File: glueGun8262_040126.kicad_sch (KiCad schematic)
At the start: 73 parts, among them CN1 KF243-5.0-2P, CN2 KF243-5.0-2P, CN3 KF243-5.0-2P, CN4 KF243-5.0-2P, CN5 KF243-5.0-2P, CN6 KF243-5.0-2P, CN7 KF243-5.0-2P, CN9 KF243-5.0-4P, Q1 SQM120P10-10m1L, U1 DRV8262DDWR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

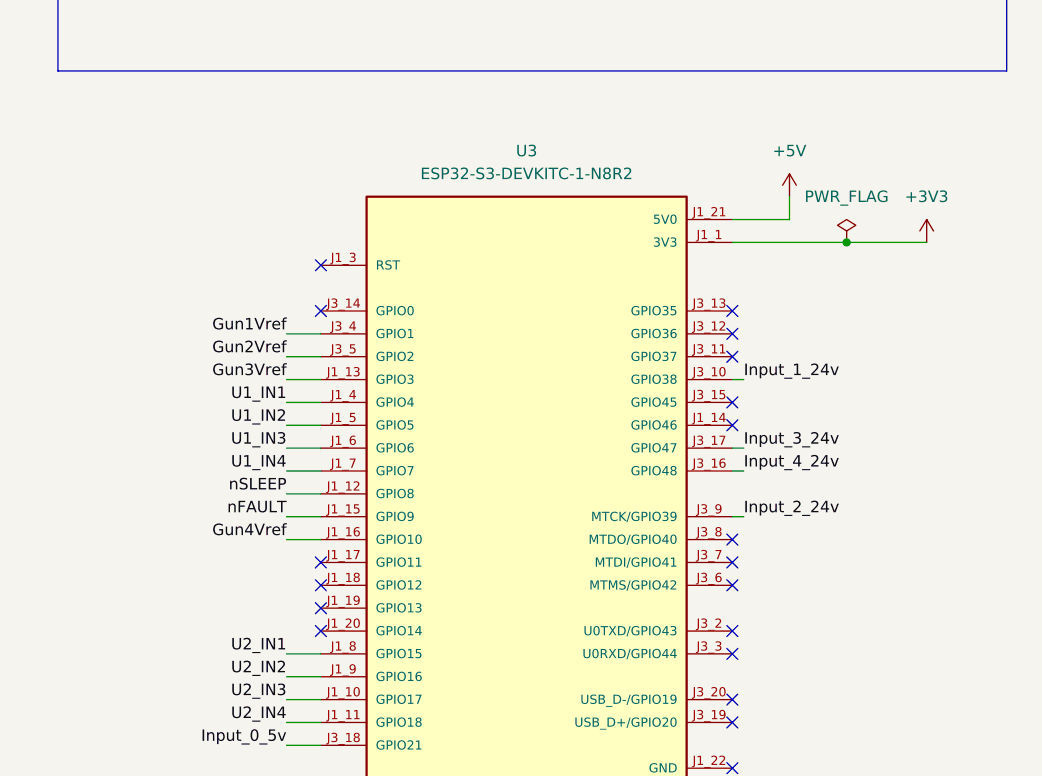
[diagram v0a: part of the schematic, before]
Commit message: schematics updated pinout
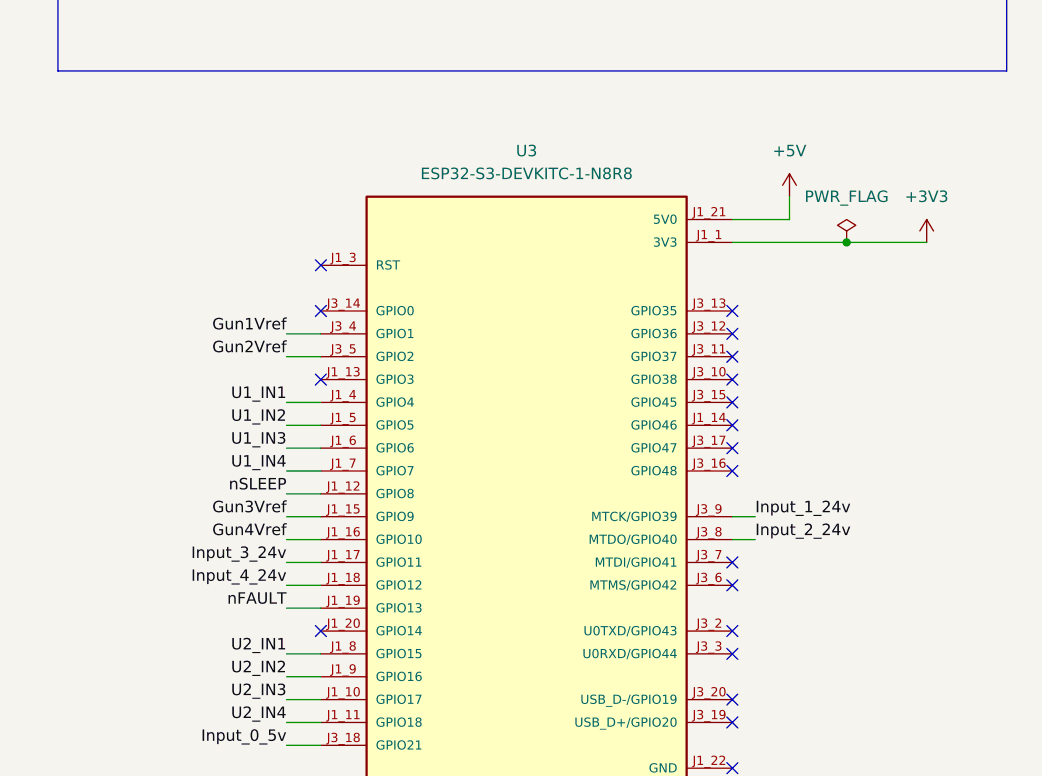
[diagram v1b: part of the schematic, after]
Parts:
- U3: value ESP32-S3-DEVKITC-1-N8R2 -> ESP32-S3-DEVKITC-1-N8R8
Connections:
- net Gun3Vref: now also U3.J1_15 (GPIO9); no longer U3.J1_13 (GPIO3)
- net Input_1_24v: now also U3.J3_9 (MTCK/GPIO39); no longer U3.J3_10 (GPIO38)
- net Input_2_24v: now also U3.J3_8 (MTDO/GPIO40); no longer U3.J3_9 (MTCK/GPIO39)
- net Input_3_24v: now also U3.J1_17 (GPIO11); no longer U3.J3_17 (GPIO47)
- net Input_4_24v: now also U3.J1_18 (GPIO12); no longer U3.J3_16 (GPIO48)
- net nFAULT: now also U3.J1_19 (GPIO13); no longer U3.J1_15 (GPIO9)

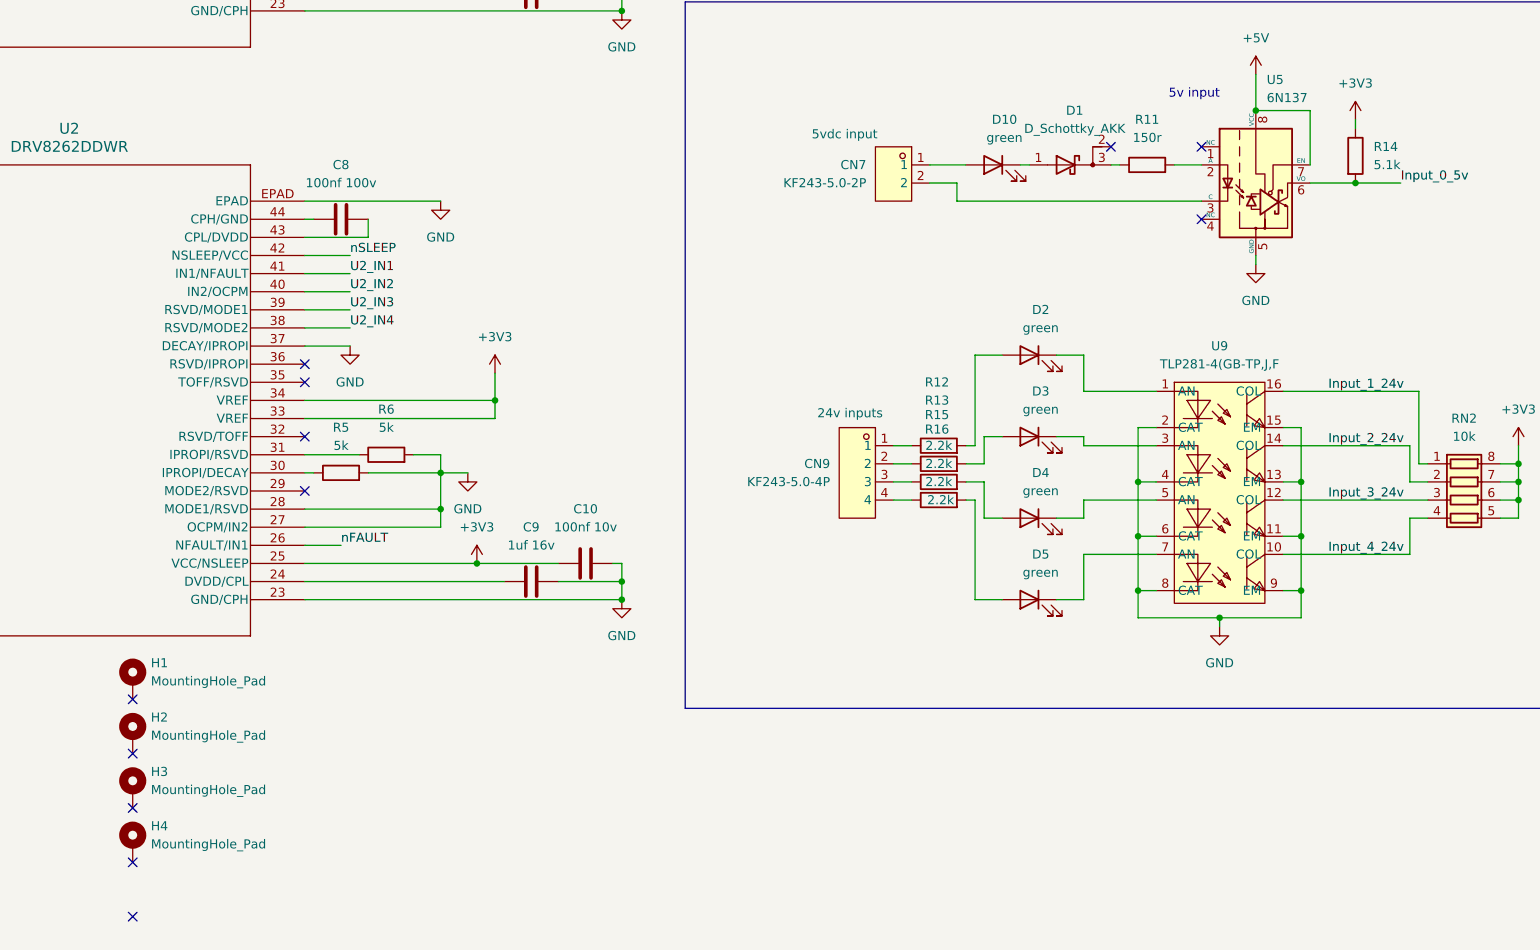
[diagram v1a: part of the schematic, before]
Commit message: pcb rewired new pinout
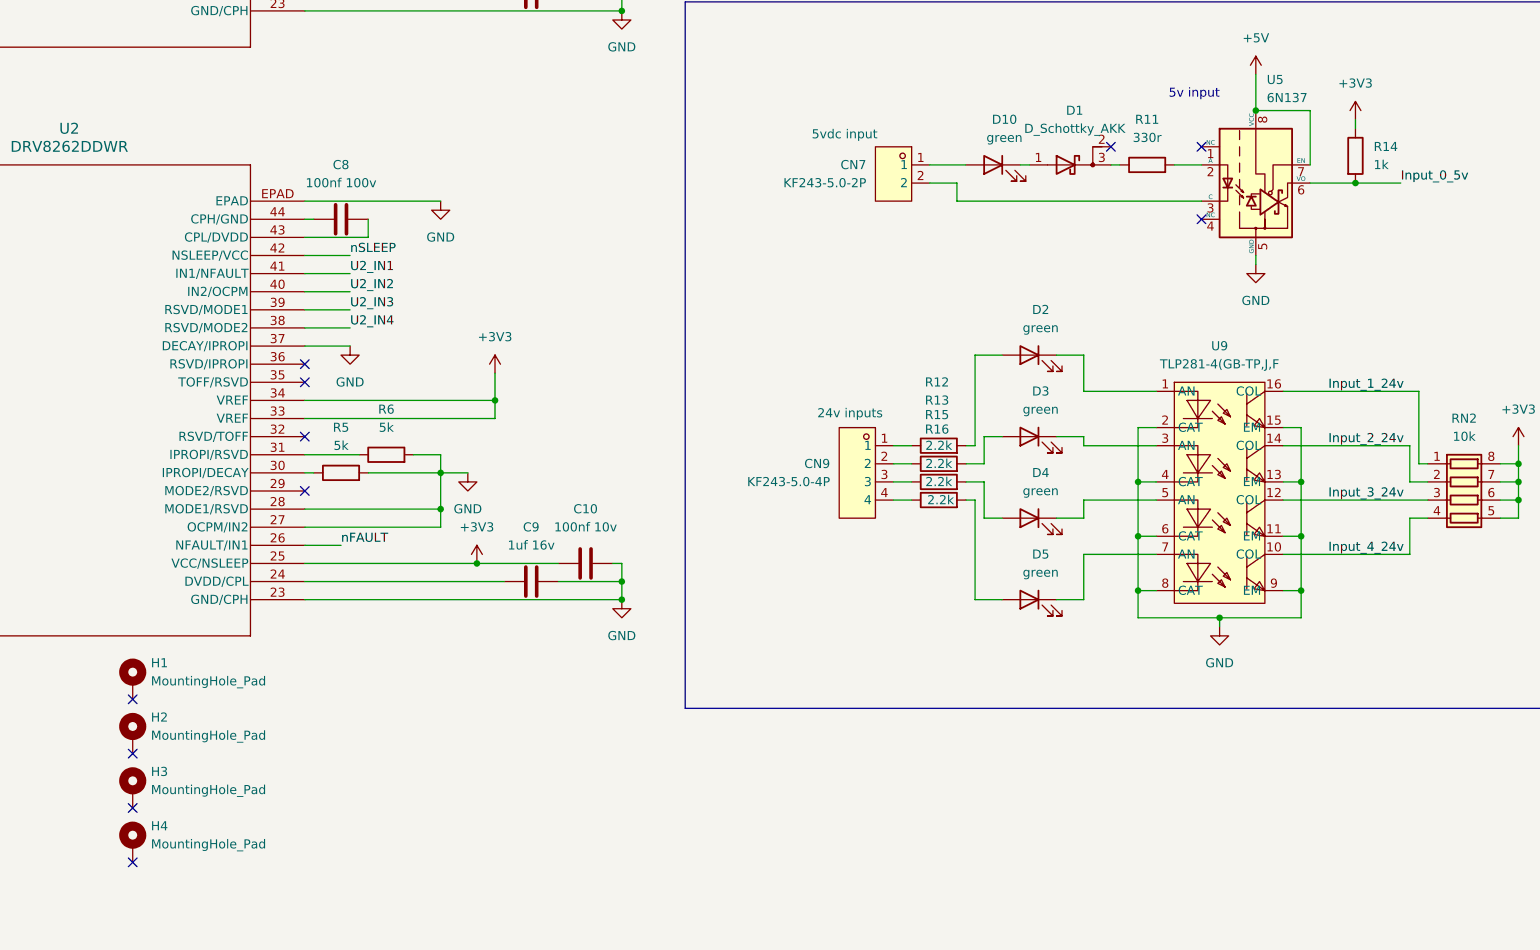
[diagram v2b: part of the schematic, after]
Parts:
- D1: footprint Package_TO_SOT_SMD:SOT-23 -> Diode_SMD:D_SOD-123; part (none) -> ss14
- D11: part (none) -> ss26
- D14: footprint (none) -> Diode_SMD:D_SMA
- R11: value 150r -> 330r
- R14: value 5.1k -> 1k; lcsc C25905 -> (none)
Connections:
- no-connect marks 39 -> 38

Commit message: redesigned before freerouting
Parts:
- D1: value D_Schottky_AKK -> reverse protection; footprint Diode_SMD:D_SOD-123 -> Diode_SMD:D_SMA; symbol Device:D_Schottky_AKK -> Device:D_Schottky
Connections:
- net at R11.1: now also D1.1 (K); no longer D1.3 (K)
- net at D10.1 (K): now also D1.2 (A); no longer D1.1 (A)
- no-connect marks 38 -> 37
